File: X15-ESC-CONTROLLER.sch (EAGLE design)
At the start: 33 parts, among them Q4 220mA/50V/3.5Ω, Y1 ECS-80-S-4X

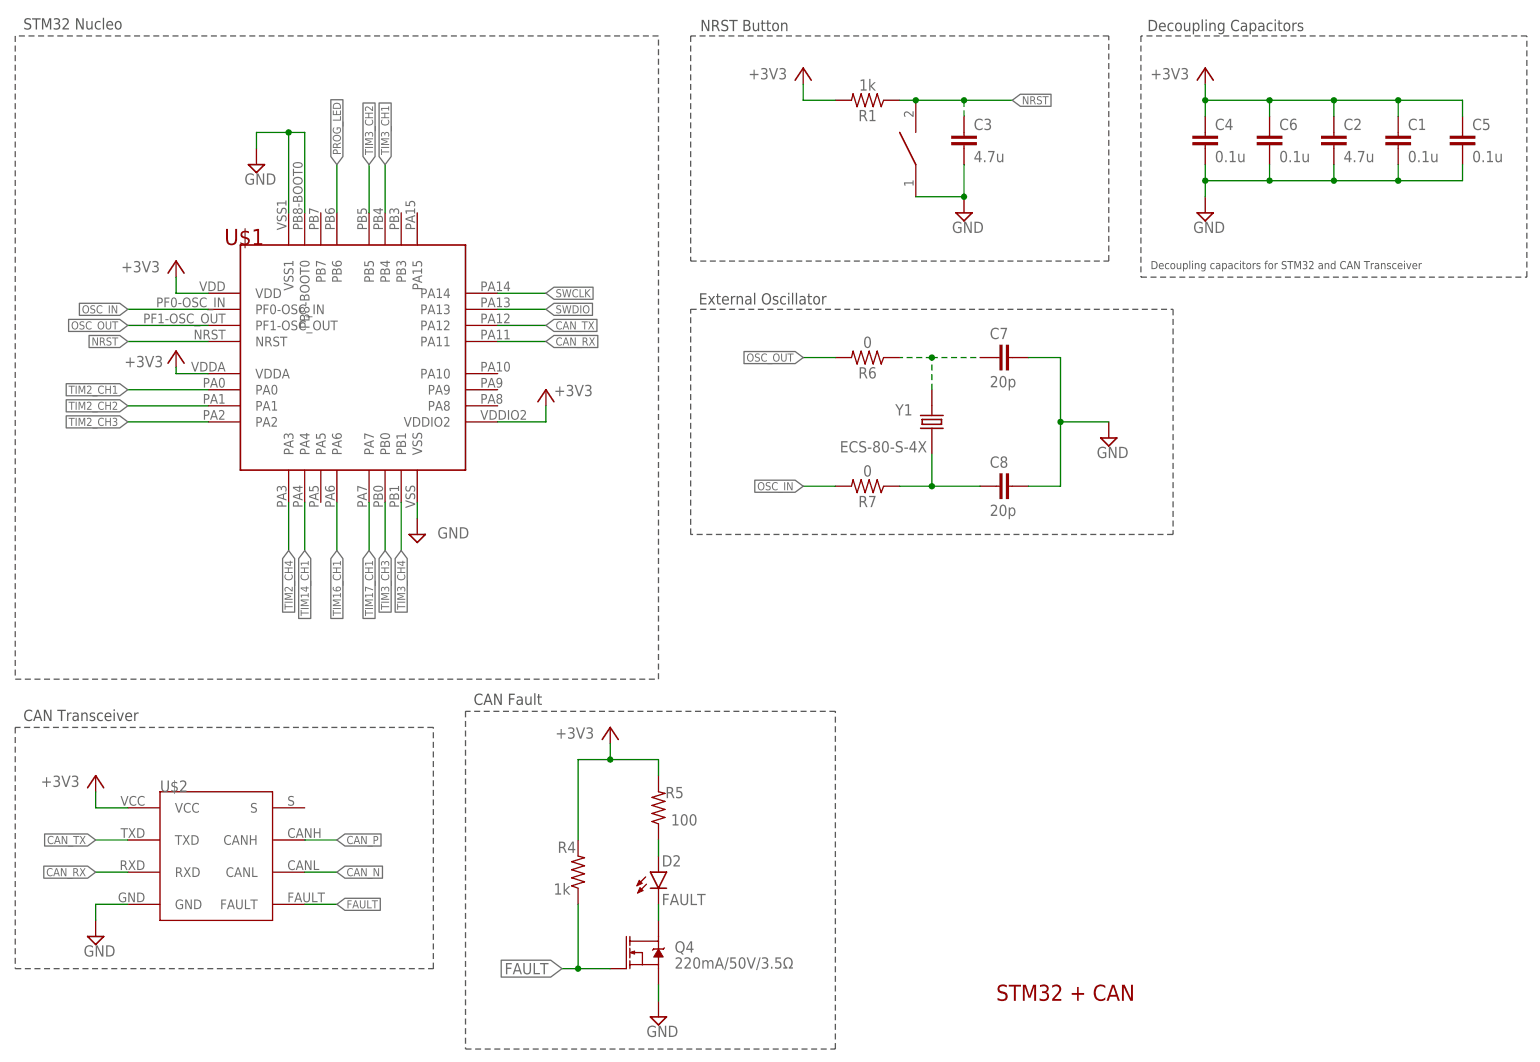
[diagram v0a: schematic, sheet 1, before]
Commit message: Fix New Version of X15-ESC Controller
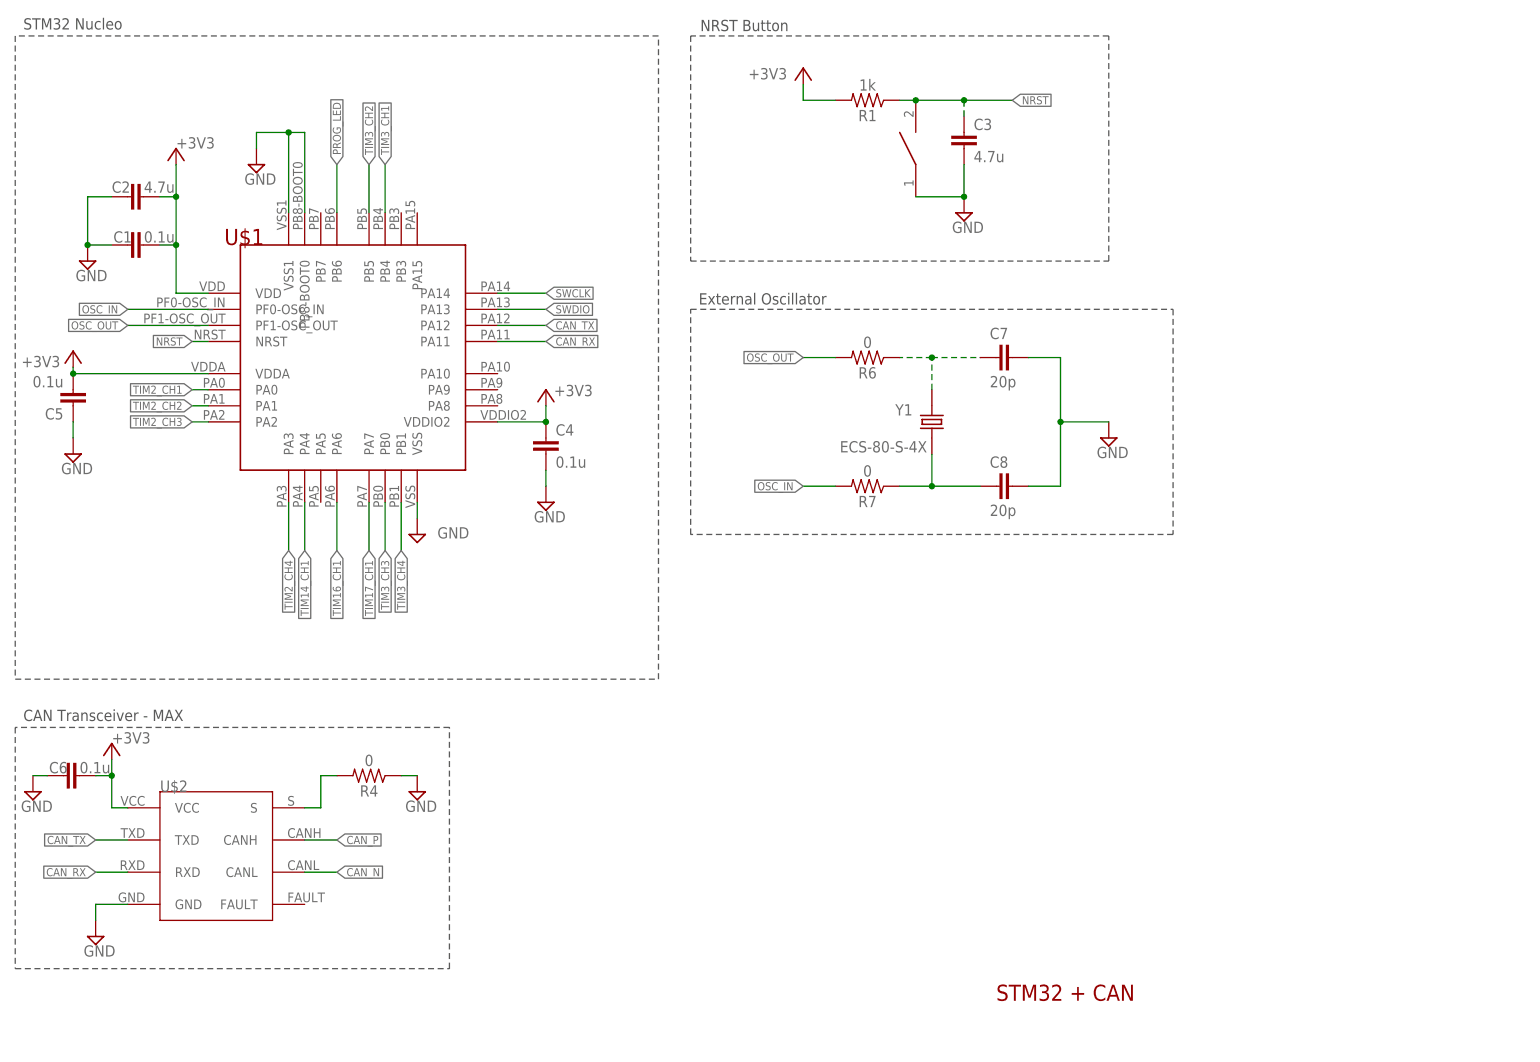
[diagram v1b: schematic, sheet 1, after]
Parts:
- removed D2: FAULT, LED-0805:LED-0805
- removed Q4: 220mA/50V/3.5Ω, SparkFun-DiscreteSemi:MOSFET-NCH-BSS138
- removed R5: 100, SparkFun-Resistors:RESISTOR0603
- R4: value 1k -> 0; device SparkFun-Resistors:RESISTOR0603 -> SparkFun-Resistors:1KOHM-0603-1/10W-1%
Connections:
- removed net FAULT: Q4.G, R4.1, U$2.FAULT
- removed net N$3: D2.A, R5.1
- net +3V3: now also C2.2, C5.1, C6.2; no longer C2.1, C5.2, C6.1, R4.2, R5.2
- net GND: now also C2.1, C5.2, C6.1, R4.1; no longer C2.2, C5.1, C6.2, Q4.S
- net N$2: now also R4.2, U$2.S; no longer D2.C, Q4.D
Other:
- note added: "CAN Transceiver - MAX"
- note removed: "CAN Fault"
- note removed: "CAN Transceiver"
- note removed: "Decoupling Capacitors"
- note removed: "Decoupling capacitors for STM32 and CAN Transceiver"
- moved on the sheet: C1, C2, C4, C5, C6, R4

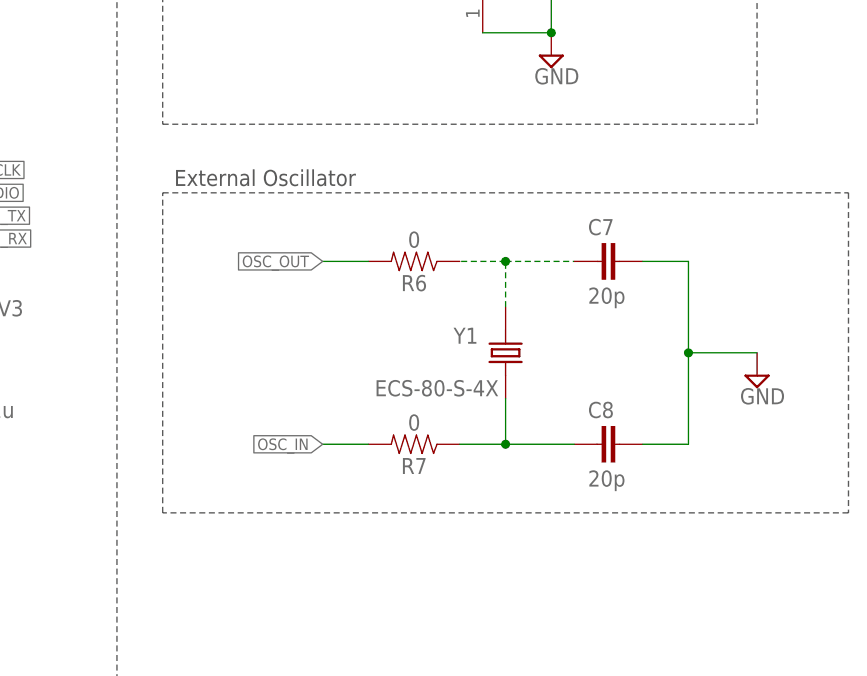
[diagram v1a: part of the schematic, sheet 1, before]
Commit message: Complete New Version of X15 ESC Controller Board
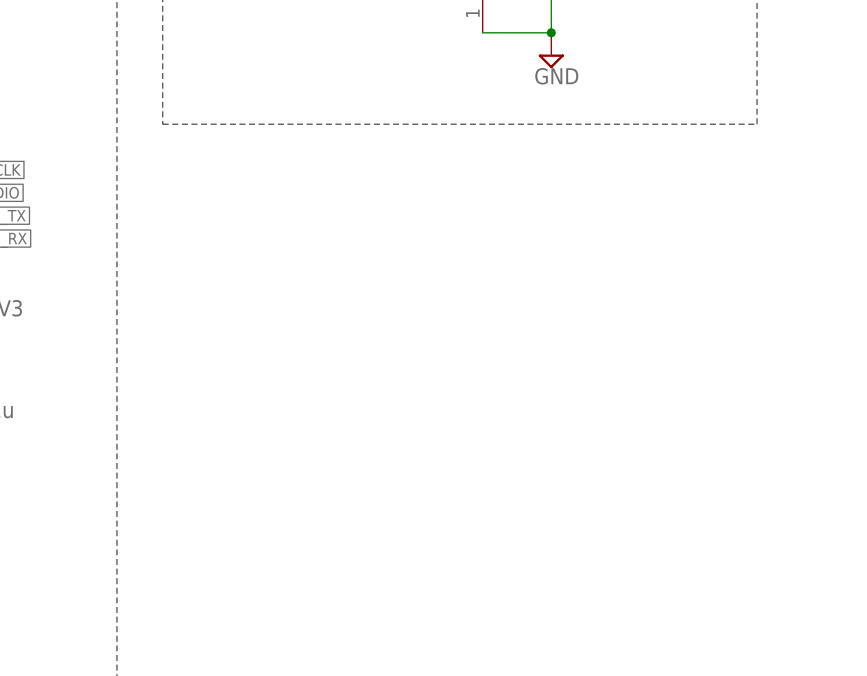
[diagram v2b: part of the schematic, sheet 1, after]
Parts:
- removed C7, C8: 20p, SparkFun-Capacitors:22PF-0603-50V-5%
- removed R6, R7: 0, SparkFun-Resistors:1KOHM-0603-1/10W-1%
- removed Y1: ECS-80-S-4X, X15-ESC-Controller-Parts-Library:ECS-80-S-4X
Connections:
- removed net N$4: C7.1, R6.1, Y1.2
- removed net N$7: C8.1, R7.1, Y1.1
- net GND: no longer C7.2, C8.2
- net OSC_IN: no longer R7.2
- net OSC_OUT: no longer R6.2
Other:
- note removed: "External Oscillator"
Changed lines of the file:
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@@
 <part name="+3V4" library="supply1" library_urn="urn:adsk.eagle:library:371" deviceset="+3V3" device=""/>
 <part name="+3V5" library="supply1" library_urn="urn:adsk.eagle:library:371" deviceset="+3V3" device=""/>
-<part name="SUPPLY13" library="supply2" library_urn="urn:adsk.eagle:library:372" deviceset="GND" device=""/>
-<part name="Y1" library="X15-ESC-Controller-Parts-Library" deviceset="ECS-80-S-4X" device=""/>
 <part name="FRAME1" library="frames" library_urn="urn:adsk.eagle:library:229" deviceset="A4L-LOC" device="" value="?"/>
 <part name="FRAME2" library="frames" library_urn="urn:adsk.eagle:library:229" deviceset="A4L-LOC" device=""/>
@@
 <part name="C1" library="SparkFun-Capacitors" deviceset="0.1UF" device="-0603-25V-5%" value="0.1u"/>
 <part name="+3V1" library="supply1" library_urn="urn:adsk.eagle:library:371" deviceset="+3V3" device=""/>
-<part name="R6" library="SparkFun-Resistors" library_urn="urn:adsk.eagle:library:532" deviceset="1KOHM" device="-0603-1/10W-1%" package3d_urn="urn:adsk.eagle:package:39650/1" value="0"/>
-<part name="R7" library="SparkFun-Resistors" library_urn="urn:adsk.eagle:library:532" deviceset="1KOHM" device="-0603-1/10W-1%" package3d_urn="urn:adsk.eagle:package:39650/1" value="0"/>
 <part name="C5" library="SparkFun-Capacitors" deviceset="0.1UF" device="-0603-25V-(+80/-20%)" value="0.1u"/>
 <part name="C3" library="SparkFun-Capacitors" deviceset="4.7UF" device="-0603-6.3V-(10%)" value="4.7u"/>
@@
 <part name="D1" library="X15-ESC-Controller-Parts-Library" deviceset="LED-0805" device="" value="PROG"/>
 <part name="J1" library="SparkFun-Connectors" library_urn="urn:adsk.eagle:library:513" deviceset="CONN_05" device="" package3d_urn="urn:adsk.eagle:package:38104/1"/>
-<part name="C7" library="SparkFun-Capacitors" library_urn="urn:adsk.eagle:library:510" deviceset="22PF" device="-0603-50V-5%" package3d_urn="urn:adsk.eagle:package:37414/1" value="20p"/>
-<part name="C8" library="SparkFun-Capacitors" library_urn="urn:adsk.eagle:library:510" deviceset="22PF" device="-0603-50V-5%" package3d_urn="urn:adsk.eagle:package:37414/1" value="20p"/>
 <part name="J5" library="SparkFun-Connectors" library_urn="urn:adsk.eagle:library:513" deviceset="CONN_03" device="" package3d_urn="urn:adsk.eagle:package:38063/1"/>
 <part name="J6" library="SparkFun-Connectors" library_urn="urn:adsk.eagle:library:513" deviceset="CONN_02" device="" package3d_urn="urn:adsk.eagle:package:38039/1"/>
@@
 <plain>
 <text x="-77.47" y="34.036" size="1.778" layer="97">CAN Transceiver - MAX</text>
-<text x="29.21" y="99.822" size="1.778" layer="97">External Oscillator</text>
 <text x="29.464" y="143.002" size="1.778" layer="97">NRST Button</text>
 <text x="76.2" y="-10.16" size="2.54" layer="94">STM32 + CAN</text>
@@
 <wire x1="93.98" y1="106.68" x2="93.98" y2="142.24" width="0.1524" layer="97" style="longdash"/>
 <wire x1="93.98" y1="142.24" x2="27.94" y2="142.24" width="0.1524" layer="97" style="longdash"/>
-<wire x1="27.94" y1="99.06" x2="104.14" y2="99.06" width="0.1524" layer="97" style="longdash"/>
-<wire x1="104.14" y1="99.06" x2="104.14" y2="63.5" width="0.1524" layer="97" style="longdash"/>
-<wire x1="104.14" y1="63.5" x2="27.94" y2="63.5" width="0.1524" layer="97" style="longdash"/>
-<wire x1="27.94" y1="63.5" x2="27.94" y2="99.06" width="0.1524" layer="97" style="longdash"/>
 <wire x1="-78.74" y1="33.02" x2="-78.74" y2="-5.08" width="0.1524" layer="97" style="longdash"/>
 <wire x1="-78.74" y1="-5.08" x2="-10.16" y2="-5.08" width="0.1524" layer="97" style="longdash"/>
@@
 <attribute name="VALUE" x="6.35" y="85.344" size="1.778" layer="96"/>
 </instance>
-<instance part="SUPPLY13" gate="GND" x="93.98" y="78.74" smashed="yes">
-<attribute name="VALUE" x="92.075" y="75.565" size="1.778" layer="96"/>
-</instance>
-<instance part="Y1" gate="G$1" x="66.04" y="81.28" smashed="yes" rot="R90">
-<attribute name="NAME" x="62.99693125" y="84.071540625" size="1.77991875" layer="95" rot="R180"/>
-<attribute name="VALUE" x="65.28303125" y="78.23733125" size="1.78006875" layer="96" rot="R180"/>
-</instance>
 <instance part="FRAME1" gate="G$1" x="-91.44" y="-22.86" smashed="yes">
 <attribute name="DRAWING_NAME" x="125.73" y="-7.62" size="2.54" layer="94"/>
@@
 <attribute name="VALUE" x="-53.34" y="124.46" size="1.778" layer="96"/>
 </instance>
-<instance part="R6" gate="G$1" x="55.88" y="91.44" smashed="yes" rot="R180">
-<attribute name="NAME" x="55.88" y="89.916" size="1.778" layer="95" font="vector" rot="R180" align="bottom-center"/>
-<attribute name="VALUE" x="55.88" y="92.964" size="1.778" layer="96" font="vector" rot="R180" align="top-center"/>
-</instance>
-<instance part="R7" gate="G$1" x="55.88" y="71.12" smashed="yes" rot="R180">
-<attribute name="NAME" x="55.88" y="69.596" size="1.778" layer="95" font="vector" rot="R180" align="bottom-center"/>
-<attribute name="VALUE" x="55.88" y="72.644" size="1.778" layer="96" font="vector" rot="R180" align="top-center"/>
-</instance>
 <instance part="C5" gate="G$1" x="-69.596" y="83.82" smashed="yes">
 <attribute name="NAME" x="-71.12" y="83.439" size="1.778" layer="95" font="vector" rot="R180"/>
@@
 </instance>
 <instance part="U$7" gate="G$1" x="63.5" y="124.46" smashed="yes" rot="R90"/>
-<instance part="C7" gate="G$1" x="78.74" y="91.44" smashed="yes" rot="R90">
-<attribute name="NAME" x="75.184" y="94.361" size="1.778" layer="95" font="vector"/>
-<attribute name="VALUE" x="75.184" y="86.741" size="1.778" layer="96" font="vector"/>
-</instance>
-<instance part="C8" gate="G$1" x="78.74" y="71.12" smashed="yes" rot="R90">
-<attribute name="NAME" x="75.184" y="74.041" size="1.778" layer="95" font="vector"/>
-<attribute name="VALUE" x="75.184" y="66.421" size="1.778" layer="96" font="vector"/>
-</instance>
 <instance part="SUPPLY7" gate="GND" x="-67.31" y="106.68" smashed="yes">
 <attribute name="VALUE" x="-69.215" y="103.505" size="1.778" layer="96"/>
@@
 </segment>
 <segment>
-<wire x1="81.28" y1="91.44" x2="86.36" y2="91.44" width="0.1524" layer="91"/>
-<wire x1="86.36" y1="91.44" x2="86.36" y2="81.28" width="0.1524" layer="91"/>
-<wire x1="86.36" y1="81.28" x2="86.36" y2="71.12" width="0.1524" layer="91"/>
-<wire x1="86.36" y1="71.12" x2="81.28" y2="71.12" width="0.1524" layer="91"/>
-<pinref part="SUPPLY13" gate="GND" pin="GND"/>
-<wire x1="93.98" y1="81.28" x2="86.36" y2="81.28" width="0.1524" layer="91"/>
-<junction x="86.36" y="81.28"/>
-<pinref part="C7" gate="G$1" pin="2"/>
-<pinref part="C8" gate="G$1" pin="2"/>
-</segment>
-<segment>
 <pinref part="U$1" gate="G$1" pin="VSS1"/>
 <wire x1="-35.56" y1="127" x2="-35.56" y2="114.3" width="0.1524" layer="91"/>
@@
 </segment>
 </net>
-<net name="N$7" class="0">
-<segment>
-<wire x1="66.04" y1="76.2" x2="66.04" y2="71.12" width="0.1524" layer="91"/>
-<wire x1="66.04" y1="71.12" x2="73.66" y2="71.12" width="0.1524" layer="91"/>
-<pinref part="Y1" gate="G$1" pin="1"/>
-<wire x1="66.04" y1="71.12" x2="60.96" y2="71.12" width="0.1524" layer="91"/>
-<junction x="66.04" y="71.12"/>
-<pinref part="R7" gate="G$1" pin="1"/>
-<pinref part="C8" gate="G$1" pin="1"/>
-</segment>
-</net>
 <net name="TIM2_CH3" class="0">
 <segment>
@@
 <label x="-60.96" y="99.06" size="1.27" layer="95" rot="R180" xref="yes"/>
 </segment>
-<segment>
-<pinref part="R7" gate="G$1" pin="2"/>
-<wire x1="50.8" y1="71.12" x2="45.72" y2="71.12" width="0.1524" layer="91"/>
-<label x="45.72" y="71.12" size="1.27" layer="95" rot="R180" xref="yes"/>
-</segment>
 </net>
 <net name="OSC_OUT" class="0">
@@
 <label x="-60.96" y="96.52" size="1.27" layer="95" rot="R180" xref="yes"/>
 </segment>
-<segment>
-<pinref part="R6" gate="G$1" pin="2"/>
-<wire x1="50.8" y1="91.44" x2="45.72" y2="91.44" width="0.1524" layer="91"/>
-<label x="45.72" y="91.44" size="1.27" layer="95" rot="R180" xref="yes"/>
-</segment>
 </net>
 <net name="PROG_LED" class="0">
@@
 </segment>
 </net>
-<net name="N$4" class="0">
-<segment>
-<pinref part="Y1" gate="G$1" pin="2"/>
-<pinref part="R6" gate="G$1" pin="1"/>
-<wire x1="66.04" y1="86.36" x2="66.04" y2="91.44" width="0.1524" layer="91" style="longdash"/>
-<wire x1="66.04" y1="91.44" x2="60.96" y2="91.44" width="0.1524" layer="91" style="longdash"/>
-<pinref part="C7" gate="G$1" pin="1"/>
-<wire x1="66.04" y1="91.44" x2="73.66" y2="91.44" width="0.1524" layer="91" style="longdash"/>
-<junction x="66.04" y="91.44"/>
-</segment>
-</net>
